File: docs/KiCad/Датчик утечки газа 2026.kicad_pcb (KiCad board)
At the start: 2 copper layers, 38.7 x 44.9 mm, 58 parts, among them J1 Conn_01x04_Pin, J2 Conn_01x04_Pin, J3 Conn_01x04_Pin, Q1 BC846BDW1, Q2 AO4807, U2 LMR50410, U3 ATtiny412-SS, U4 TGS_2611-E00, U5 TLIN2029ADRBRQ1, U6 LMR50410, U7 ATtiny412-SS, U8 BTS4142N

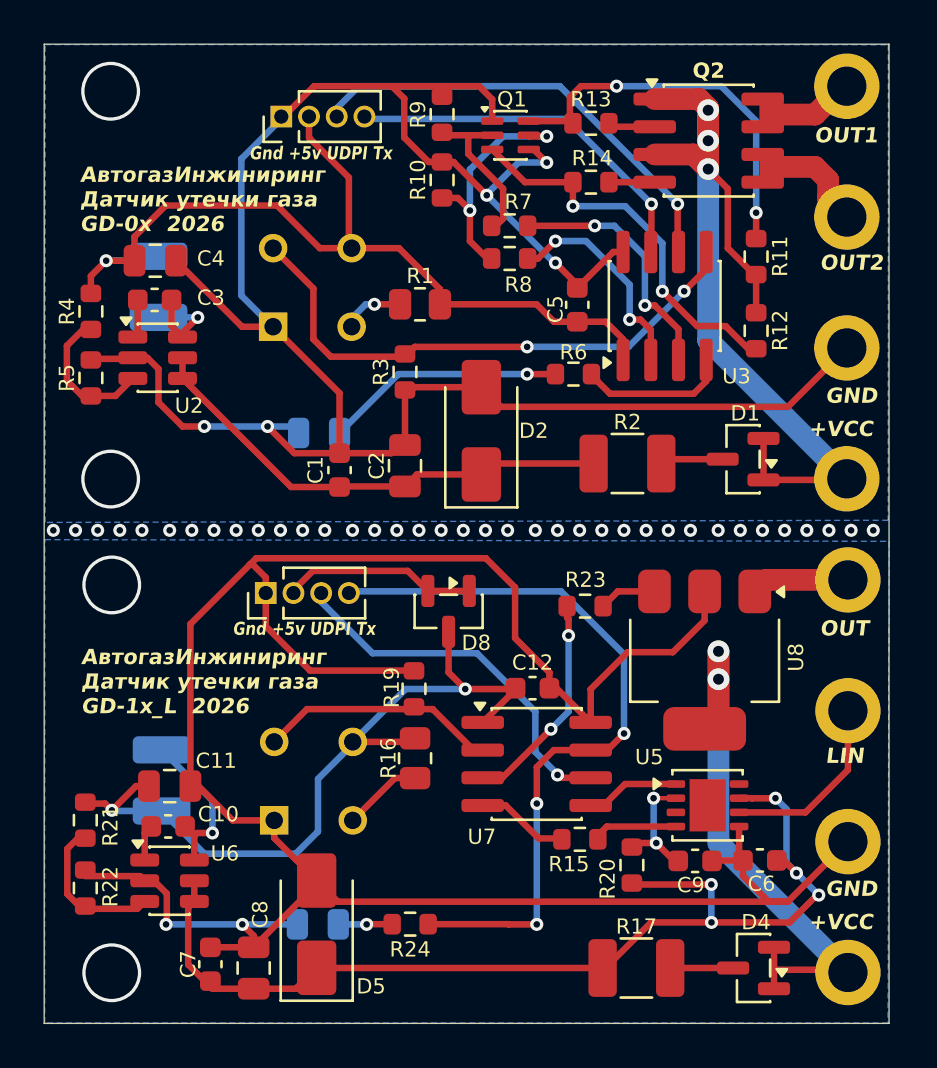
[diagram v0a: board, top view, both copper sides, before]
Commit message: Разделить платы разных версий
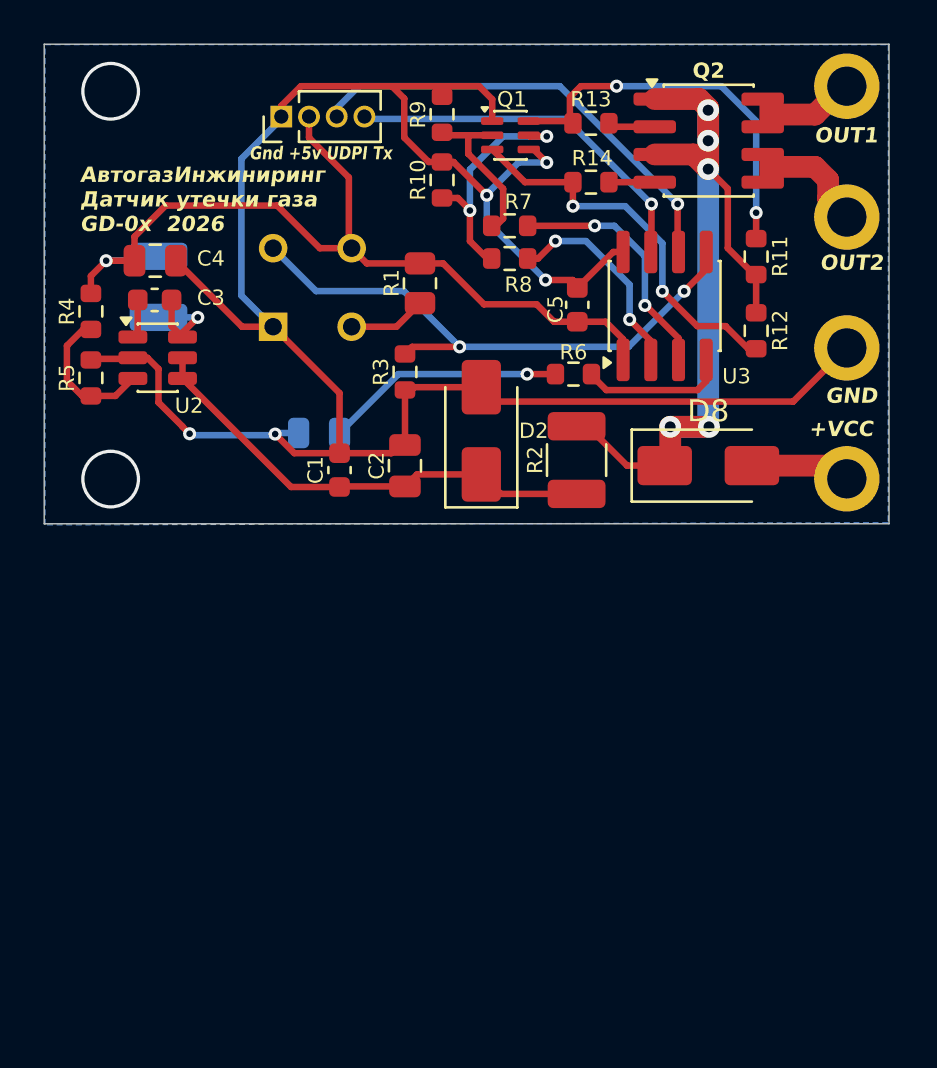
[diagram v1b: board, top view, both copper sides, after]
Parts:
- removed C10, C12, C6, C7, C9: 0.1µF, Capacitor_SMD:C_0603_1608Metric
- removed C11: 47µF10v, Capacitor_SMD:C_0805_2012Metric
- removed C8: 10µF50v, Capacitor_SMD:C_0805_2012Metric
- removed D1, D4: BAV70, Package_TO_SOT_SMD:SOT-23
- removed D5: SMAJ33A, Diode_SMD:D_SMA
- removed D6: LED RED, LED_SMD:LED_0805_2012Metric
- removed the J2 at (162.0, 106.3)
- removed J3: Conn_01x04_Pin, Connector_PinHeader_1.27mm:PinHeader_1x04_P1.27mm_Vertical
- removed L2: 4.7µH, Inductor_SMD:L_1210_3225Metric
- removed R15, R24: 470, Resistor_SMD:R_0603_1608Metric
- removed R16: 10, Resistor_SMD:R_0805_2012Metric
- removed R17: 5.1, Resistor_SMD:R_1210_3225Metric_Pad1.30x2.65mm_HandSolder
- removed R19, R23: 4.7k, Resistor_SMD:R_0603_1608Metric
- removed R20: 220k, Resistor_SMD:R_0603_1608Metric
- removed R21: 88k, Resistor_SMD:R_0603_1608Metric
- removed R22: 22k, Resistor_SMD:R_0603_1608Metric
- removed the U4 at (137.5, 97.5)
- removed U5: TLIN2029ADRBRQ1, Package_SON:VSON-8-1EP_3x3mm_P0.65mm_EP1.65x2.4mm
- removed U6: LMR50410, Package_TO_SOT_SMD:SOT-23-6
- removed U7: ATtiny412-SS, Package_SO:SOIC-8_3.9x4.9mm_P1.27mm
- removed U8: BTS4142N, Package_TO_SOT_SMD:SOT-223
- D8: value BAV70 -> MBRA360; footprint Package_TO_SOT_SMD:SOT-23 -> Diode_SMD:D_SMA
- R4: value 88k -> 82k
- moved D8 13.7 mm to (155.6, 83.1), turned to 0 degrees
- moved R2 2.34 mm to (149.6, 82.8), turned to 90 degrees
- moved R1 0.96 mm to (142.4, 74.7), turned to 90 degrees
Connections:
- D8 pad 1: Net-(J3-Pin_2) -> /+24_V
- D8 pad 2: Net-(J3-Pin_2) -> /+24V
- J2 pad 3: /out2 -> /OUT2
- J2 pad 4: /out1 -> /OUT1
- Q2 pad 1: /+24V -> /+24_V
- Q2 pad 3: /+24V -> /+24_V
- R11 pad 1: /+24V -> /+24_V
- R12 pad 1: /+24V -> /+24_V
- R2 pad 2: Net-(D1-K) -> /+24_V
- U4 pad 4: Net-(U5-VH_2) -> Net-(U1-VH_2)
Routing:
- net GND: track 210.7 -> 99.4 mm, vias 7 -> 5
- net Net-(D5-A1): track 48.6 -> 0.00 mm, vias 5 -> 0
- net /+24_V: track 0.00 -> 39.8 mm, vias 0 -> 5
- net /+24V: track 40.9 -> 4.67 mm, vias 3 -> 0
- net /Ver_LIN/+5v: track 35.5 -> 0.00 mm, vias 2 -> 0
- net /Ver_LIN/Tx: track 34.3 -> 0.00 mm, vias 3 -> 0
- net /Ver_LIN/+24V: track 25.7 -> 0.00 mm, vias 2 -> 0
- net /Ver_LIN/UPDI: track 17.4 -> 0.00 mm, vias 1 -> 0
- net /Ver_LIN/InGas: track 11.0 -> 0.00 mm
- net Net-(U7-PA7): track 10.1 -> 0.00 mm, vias 2 -> 0
- net Net-(J3-Pin_2): track 8.68 -> 0.00 mm
- net /Ver_LIN/LIN: track 8.51 -> 0.00 mm
- net Net-(U6-LX): track 7.37 -> 0.00 mm, vias 1 -> 0
- net Net-(U6-FB): track 6.87 -> 0.00 mm
- net /out2: track 6.17 -> 0.00 mm
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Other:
- board size 38.7 x 44.9 mm -> 38.7 x 22 mm
- board text removed: "LIN"
- board text removed: "OUT"
- board text removed: "АвтогазИнжиниринг Датчик утечки газа GD-1x_L 2026"
